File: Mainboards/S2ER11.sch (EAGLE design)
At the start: 52 parts, among them IC1 LD1117S33, IC2 CC1101RTK, IC3 STM32F051C8, Q1 IRLML9301, Q2 8M, X1 VCC, X2 CLK, X3 GND, X4 DIO, X5 RST, X6 NC

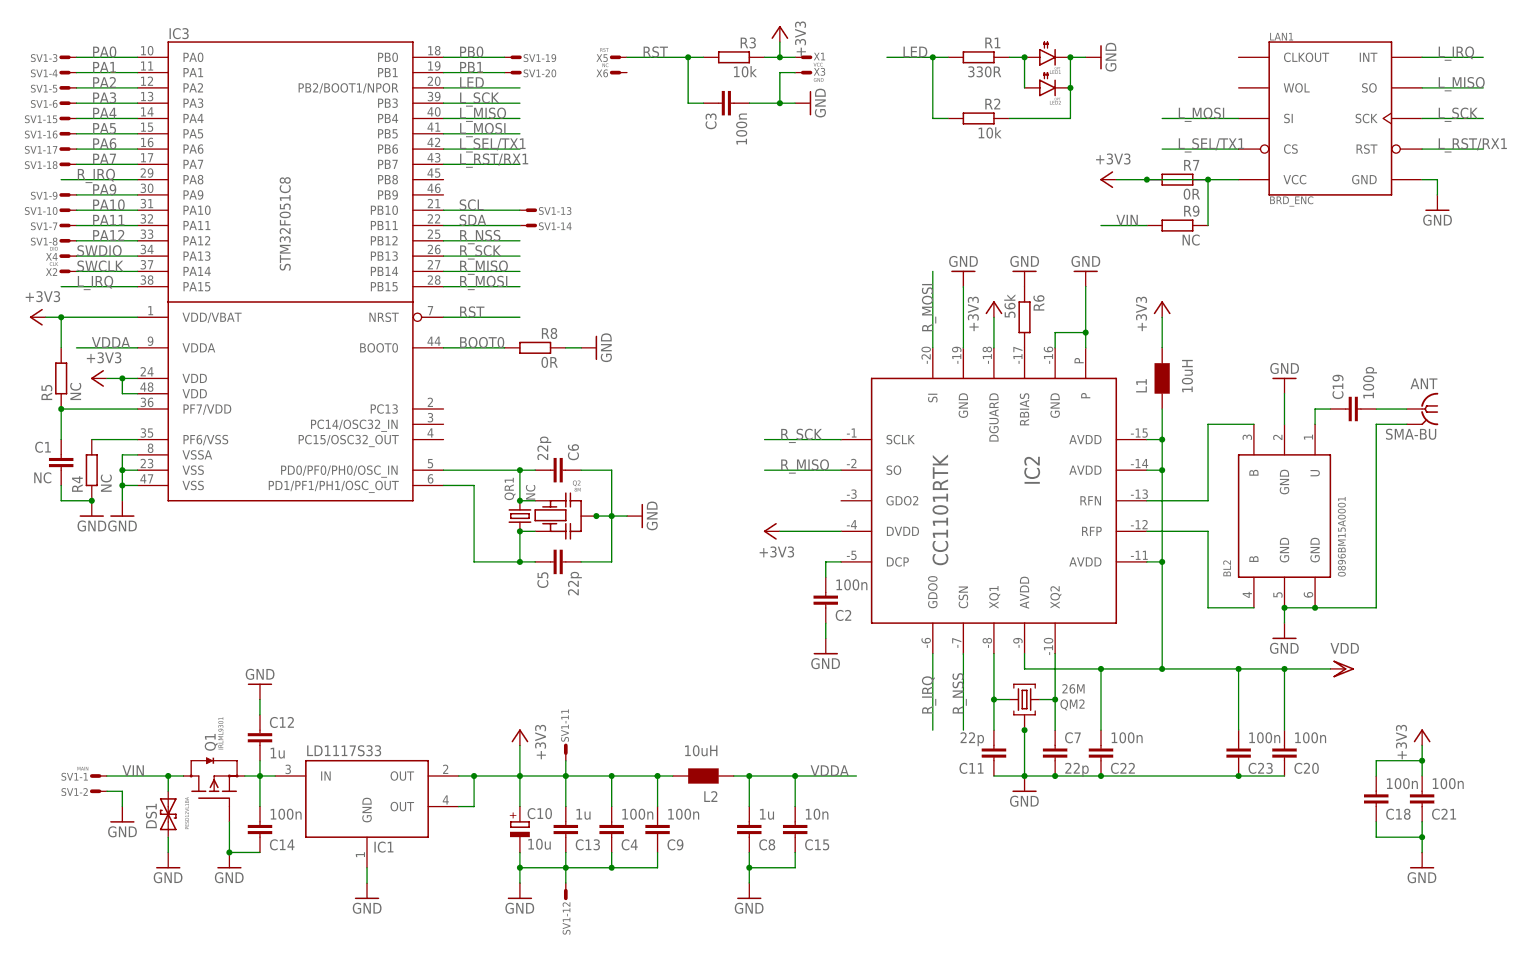
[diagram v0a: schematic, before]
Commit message: Added prototypes
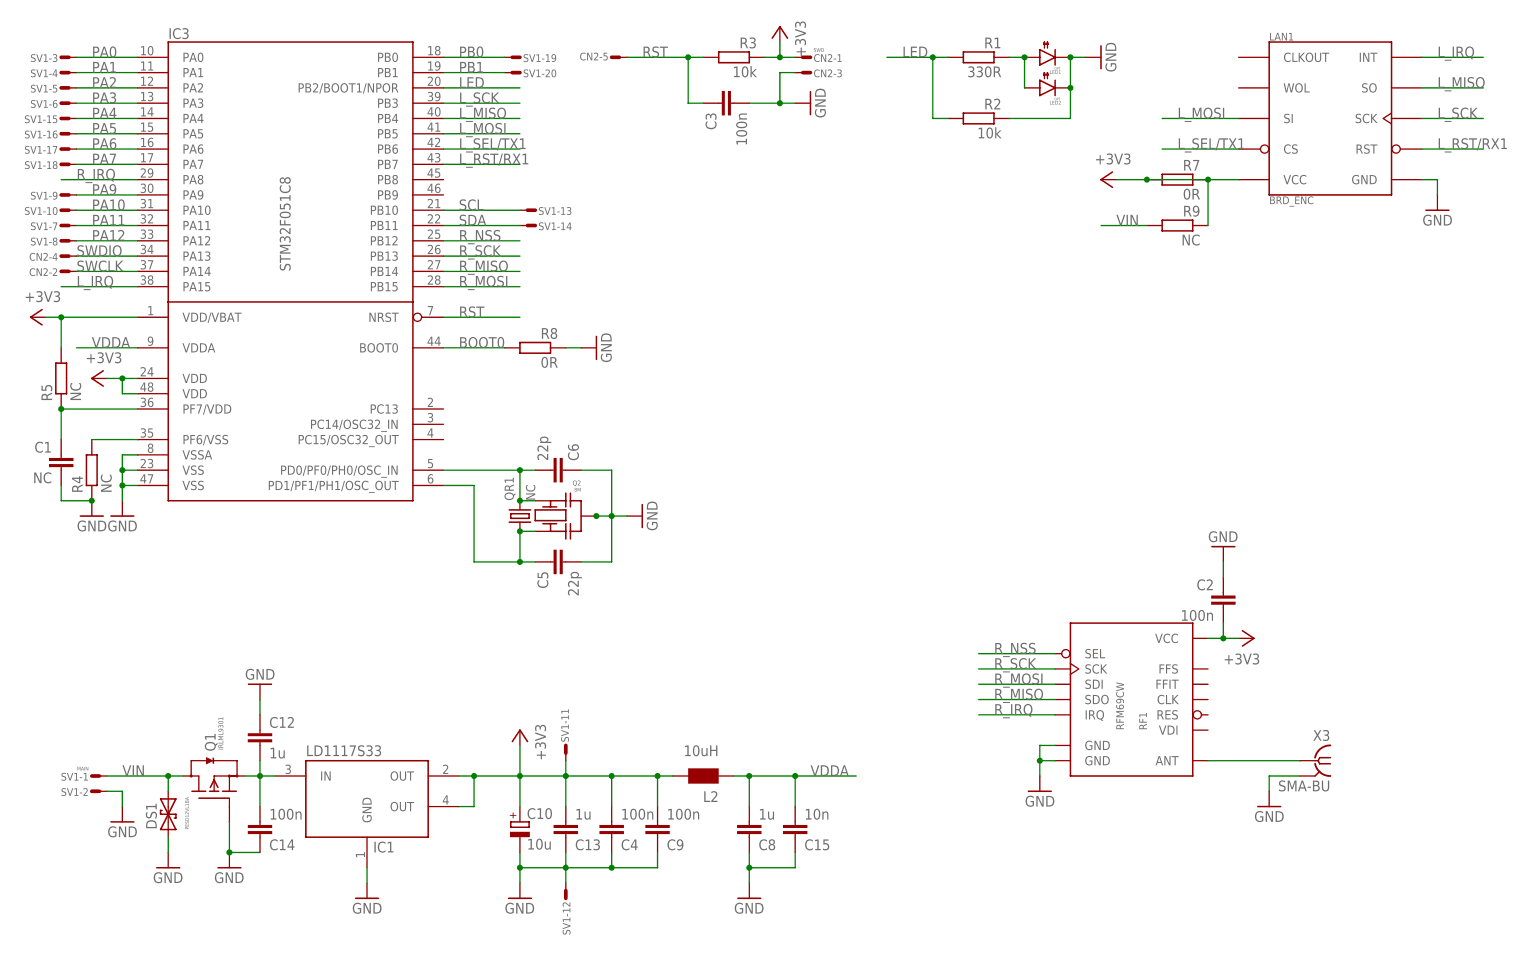
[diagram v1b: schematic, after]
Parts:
- removed ANT: SMA-BU, Conn:SMA-BU
- removed BL2: 0896BM15A0001, RF:BL
- removed C11, C7: 22p, RCL:C0603
- removed C18, C20, C21, C22, C23: 100n, RCL:C0603
- removed C19: 100p, RCL:C0603
- removed IC2: CC1101RTK, RF:CC110LV
- removed L1: 10uH, RCL:L0603
- removed QM2: 26M, QUARTZ:QM3.2X2.5
- removed R6: 56k, RCL:R0603
- removed X1: VCC, Conn:WIREPADT1.6/0.9
- removed X2: CLK, Conn:WIREPADT1.6/0.9
- removed X4: DIO, Conn:WIREPADT1.6/0.9
- removed X5: RST, Conn:WIREPADT1.6/0.9
- removed X6: NC, Conn:WIREPADT1.6/0.9
- added CN2: SWD, Conn:CON6L
- added RF1: RFM69CW, RF:RFM12B-868-S1
- X3: value GND -> SMA-BU; device Conn:WIREPADT1.6/0.9 -> Conn:SMA-BU
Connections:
- removed net N$11: C11.2, IC2.XQ1, QM2.2
- removed net N$12: C7.1, IC2.XQ2, QM2.1
- removed net N$13: BL2.U@1, C19.1
- removed net N$14: ANT.1, C19.2
- removed net N$6: IC2.RBIAS, R6.2
- removed net N$7: C2.2, IC2.DCP
- removed net N$8: BL2.B@3, IC2.RFN
- removed net N$9: BL2.B@4, IC2.RFP
- removed net VDD: C20.2, C22.2, C23.2, IC2.AVDD, IC2.AVDD@1, IC2.AVDD@2, IC2.AVDD@3, L1.1
- new net N$5: RF1.ANT, X3.1
- net +3V3: now also C2.2, CN2-1.S, RF1.VCC; no longer C18.2, C21.2, IC2.DGUARD, IC2.DVDD, L1.2, X1.S
- net GND: now also CN2-3.S, RF1.GND, RF1.GND@1, X3.2; no longer ANT.2, BL2.GND@2, BL2.GND@5, BL2.GND@6, C11.1, C18.1, C20.1, C21.1, C22.1, C23.1, C7.2, IC2.GND, IC2.GND@1, IC2.P, QM2.M1, QM2.M2, R6.1, X3.S
- net RST: now also CN2-5.S; no longer X5.S
- net R_IRQ: now also RF1.IRQ; no longer IC2.GDO0
- net R_MISO: now also RF1.SDO; no longer IC2.SO
- net R_MOSI: now also RF1.SDI; no longer IC2.SI
- net R_NSS: now also RF1.SEL; no longer IC2.CSN
- net R_SCK: now also RF1.SCK; no longer IC2.SCLK
- net SWCLK: now also CN2-2.S; no longer X2.S
- net SWDIO: now also CN2-4.S; no longer X4.S
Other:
- moved on the sheet: C2
